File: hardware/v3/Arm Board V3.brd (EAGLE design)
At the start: 165.1 x 76.2 mm, 60 parts, among them CN1 1X4-BIG, IC1 L6208D, IC2 L6208D, IC3 L6208D, Q3 Q_LTC490, U1 MAX3468CSA, U2 XBEE-1B3

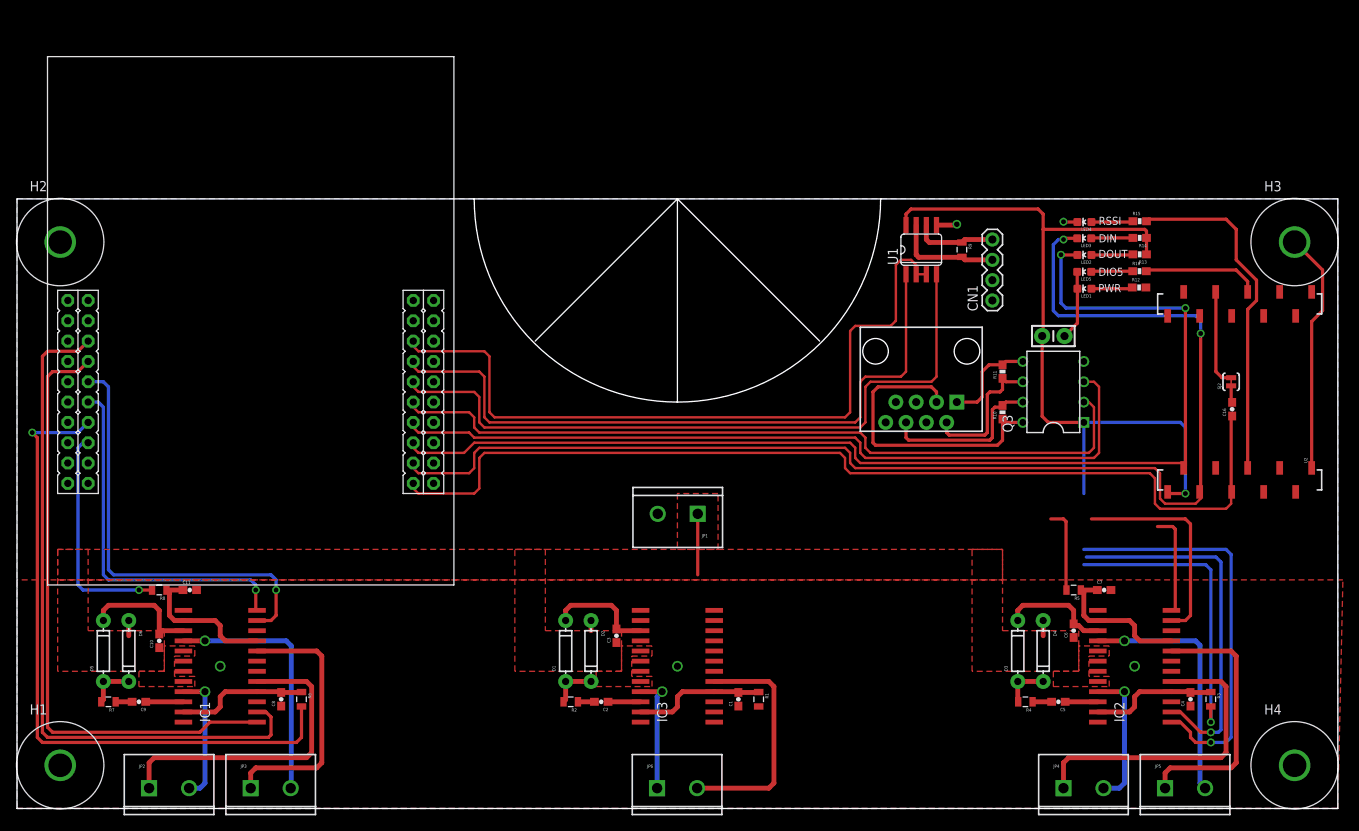
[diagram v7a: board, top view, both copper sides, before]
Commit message: Routing and Voltage Regulators (See Notes)
Started to route all of the pins towards the processor.  They need to be
reordered/reassigned since they do not make routing sense.  Added the
+12V and +18V regulators and hooked them up.  The +3V3 and +5V still
need to be picked and placed.
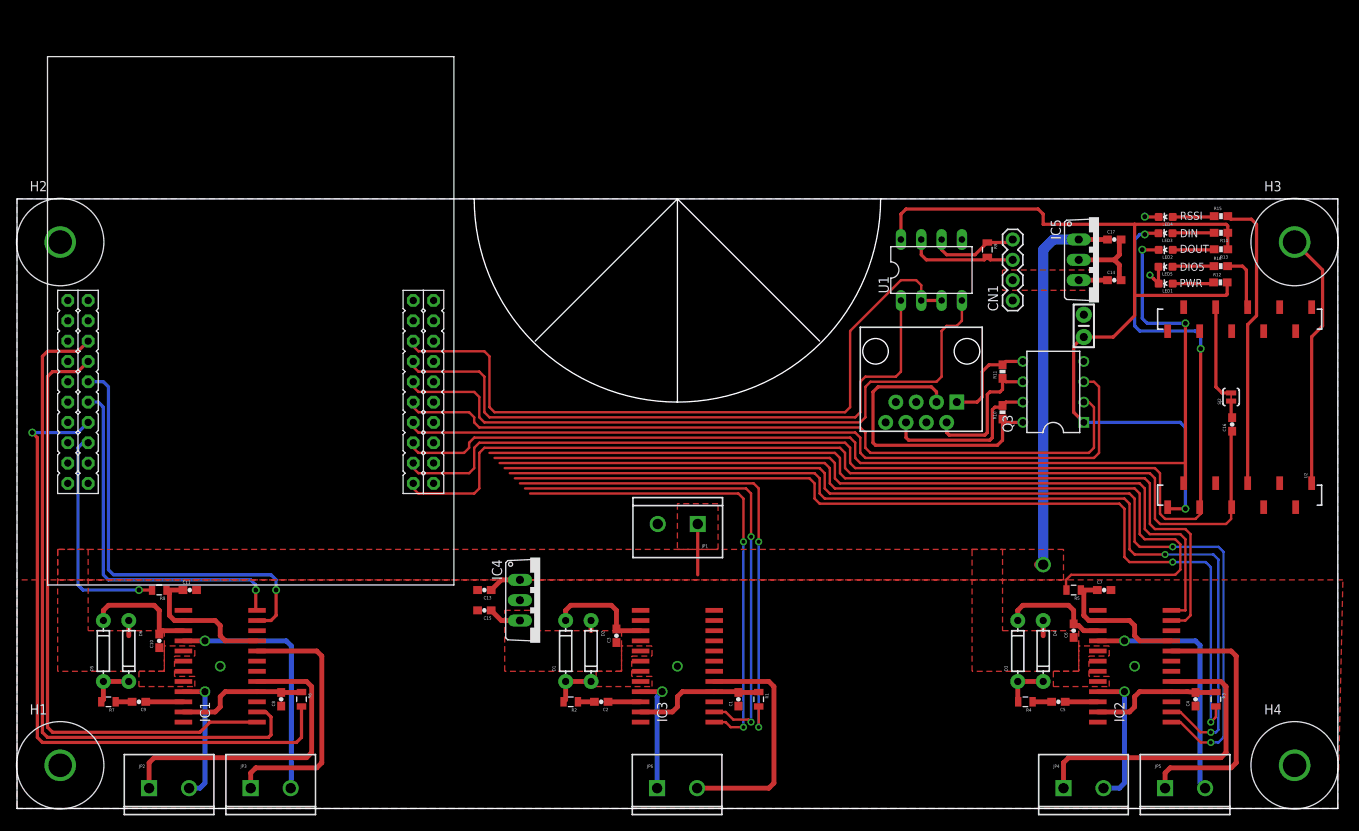
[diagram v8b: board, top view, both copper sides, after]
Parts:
- added C13, C14, C15, C17: 0.1uF, SparkFun-Capacitors:0603-CAP
- added IC4, IC5: 7812TV, linear:TO220V
- U1: value MAX3468CSA -> MAX3468CPA; device maxim:SO08 -> maxim:DIL08
- moved R16 10.2 mm to (150.5, 67.8)
- moved LED1 10.2 mm to (143.6, 65.6)
- moved LED2 10.2 mm to (143.6, 69.8)
- moved LED3 10.2 mm to (143.6, 71.9)
- moved LED4 10.2 mm to (143.6, 73.9)
- moved LED5 10.2 mm to (143.6, 67.7)
- moved R12 10.2 mm to (150.4, 65.8)
- moved R13 10.2 mm to (150.5, 69.9)
- moved R14 10.2 mm to (150.5, 72.0)
- moved R15 10.2 mm to (150.5, 74.0)
- moved C12 4.02 mm to (133.3, 60.3), turned to 90 degrees
- moved R9 3.17 mm to (121.3, 69.8)
- moved U1 2.84 mm to (114.3, 67.3)
- moved CN1 2.54 mm to (124.5, 63.5)
- moved C16 1.91 mm to (151.9, 48.0)
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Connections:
- new net +12V: C15.1, C3.1, D2.A, IC3.17, IC3.20, IC4.3
- net +18V: now also C14.1, IC5.3
- net EN_A_3: now also U$1.PB0
- net GND: now also C13.2, C14.2, C15.2, C17.2, IC4.2, IC5.2
- net IN1_A_3: now also U$1.PB1
- net IN2_A_3: now also U$1.PB2
- net VIN: now also C13.1, C17.1, IC4.1, IC5.1; no longer C3.1, D2.A, IC3.17, IC3.20
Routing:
- net EN_B_2: track 10.6 -> 112.7 mm
- net IN2_B_2: track 13.0 -> 105.3 mm
- net IN1_B_2: track 26.7 -> 108.7 mm
- net EN_A_2: track 37.1 -> 117.8 mm, vias 1 -> 2
- net IN2_A_2: track 45.4 -> 125.9 mm, vias 1 -> 2
- net IN1_A_2: track 50.7 -> 129.5 mm, vias 1 -> 2
- net EN_A_3: track 0.00 -> 62.5 mm, vias 0 -> 2
- net IN2_A_3: track 0.00 -> 62.2 mm, vias 0 -> 2
- net IN1_A_3: track 0.00 -> 59.4 mm, vias 0 -> 2
- net VIN: track 12.7 -> 62.9 mm, vias 0 -> 1
- net +3V3: track 98.2 -> 118.0 mm
- net DIO5: track 14.6 -> 7.48 mm
- net RXD3: track 143.7 -> 137.4 mm
- net RSSI: track 43.2 -> 37.2 mm
- net +12V: track 0.00 -> 5.39 mm
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- added copper zone on layer 1, net +12V
- added copper zone on layer 1, net +18V
